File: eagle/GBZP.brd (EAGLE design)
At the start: 69.5 x 114.2 mm, 44 parts, among them CN1 Battery Connection, J1 AUDIO_JACK_3.5MM_SMD, U4 LM4875, X2 HEADPHONE

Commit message: updates
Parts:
- removed C1: 10uF, adafruit:C0805
- removed C15, C18, C6, C7: 10u, rcl:C0805
- removed C17: 100n, rcl:C0805
- removed C5: 220n, rcl:C0805
- removed C8: 330n, rcl:C0805
- removed C9: 100uF, rcl:153CLV-0405
- removed R4: 270Ohm, adafruit:R0805
- removed R6: 150Ohm, adafruit:R0805
- removed R7: 27k, GBA:VOLUME
- removed R8: 270R, rcl:R0805
- removed R9: 100k, rcl:R0805
- removed SP2: SPEAKER, GBA:SPEAKER
- removed U4: LM4875, texas:SOIC8
- removed X2: HEADPHONE, GBA:HEADPHONE
- added C10, C11: 100nF, adafruit:C0805
- added C12: 10uF, adafruit:C0805
- added R10: 27k, GBA:VOLUME
- added U1: LM4875, texas:SOIC8
- C2: value 10uF -> 100uF; device adafruit:C0805 -> SparkFun-Capacitors:NIC_10X10.5_CAP
- C3: value 33nF -> 220nF
- C4: value 33nF -> 330nF
- R5: value 150Ohm -> 270Ohm
- moved SP1 117.5 mm to (91.0, 70.0)
- moved C2 106.2 mm to (105.0, 97.0), flipped to the top
- moved R5 61.8 mm to (86.0, 58.0), flipped to the top, turned to 0 degrees
- moved C3 55.9 mm to (86.0, 52.0), flipped to the top, turned to 0 degrees
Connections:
- removed net 5V: C15.1, C17.1, C18.1, C7.2, R7.5, R9.2, U4.1
- removed net N$11: C6.1, U4.7
- removed net N$13: C9.-, X2.L, X2.R
- removed net N$14: C9.+, SP2.1, U4.5
- removed net N$15: SP2.2, U4.8
- removed net N$16: R9.1, U4.3, X2.2
- removed net N$3: C2.1, C3.2, R4.2, R5.2
- removed net N$5: C5.1, C8.1, R8.2
- removed net N$8: R7.3, U4.4
- removed net N$9: C5.2, U4.2
- new net BYP: C10.1, U1.7
- new net DC_VOL: R10.3, U1.4
- new net HEADPHONES: J1.RING, J1.TIP, R5.1, U1.3
- new net VIN: C3.1, U1.2
- new net VOUT1: C2.+, SP1.P$1, U1.5
- new net VOUT2: SP1.P$2, U1.8
- net GND: now also C10.2, R10.1, U1.6; no longer C15.2, C17.2, C18.2, C3.1, C6.2, C7.1, C8.2, R5.1, R6.2, R7.1, U4.6, X2.1, X2.GND
- net N$1: now also C2.-, J1.RSH, J1.TSH; no longer C1.2, J1.RING
- net N$2: now also C3.2, C4.2, R3.2; no longer C2.2, J1.TIP
- net N$4: now also C11.2, C12.2, U1.1; no longer C1.1, C4.2, R3.2, R6.1
- net PWM: no longer R8.1
- net PWM_LEFT: no longer R4.1
- net SWITCH_OUT+: now also C11.1, C12.1, R10.5, R5.2
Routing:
- net N$2: track 18.3 -> 0.00 mm
- net N$1: track 13.4 -> 0.00 mm
- net N$4: track 6.45 -> 0.00 mm
- net N$3: track 6.45 -> 0.00 mm
- net PWM_LEFT: track 80.4 -> 77.4 mm

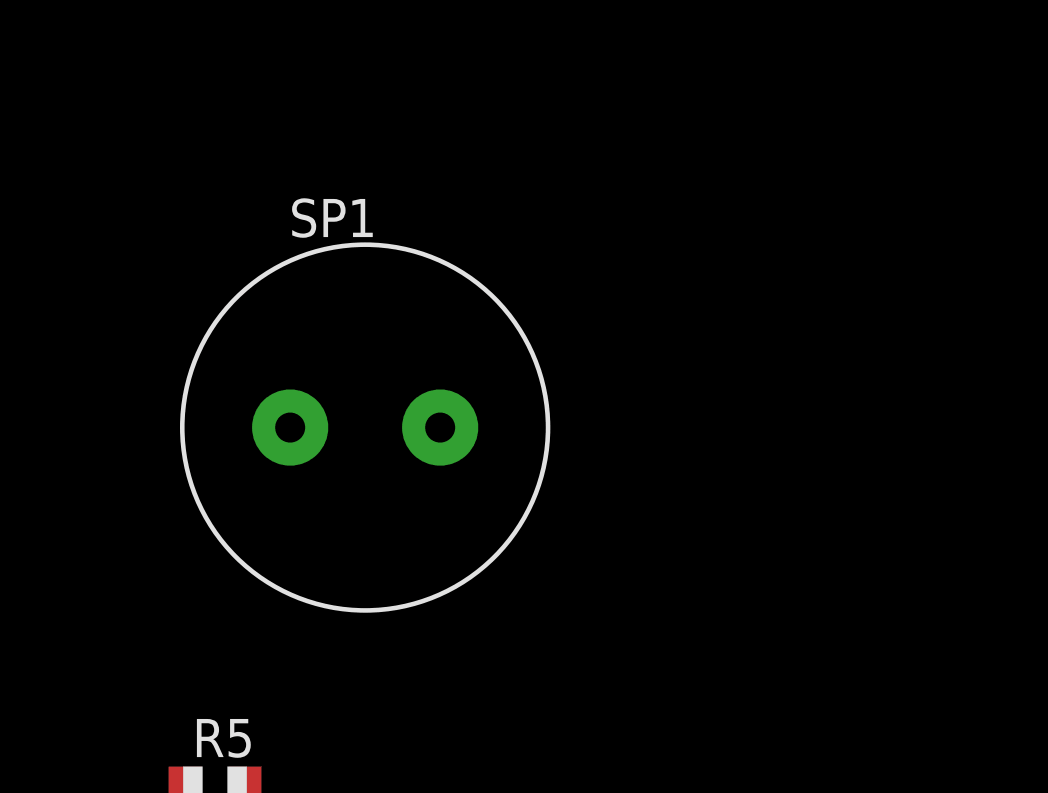
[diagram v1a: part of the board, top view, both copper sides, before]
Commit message: added LM4875
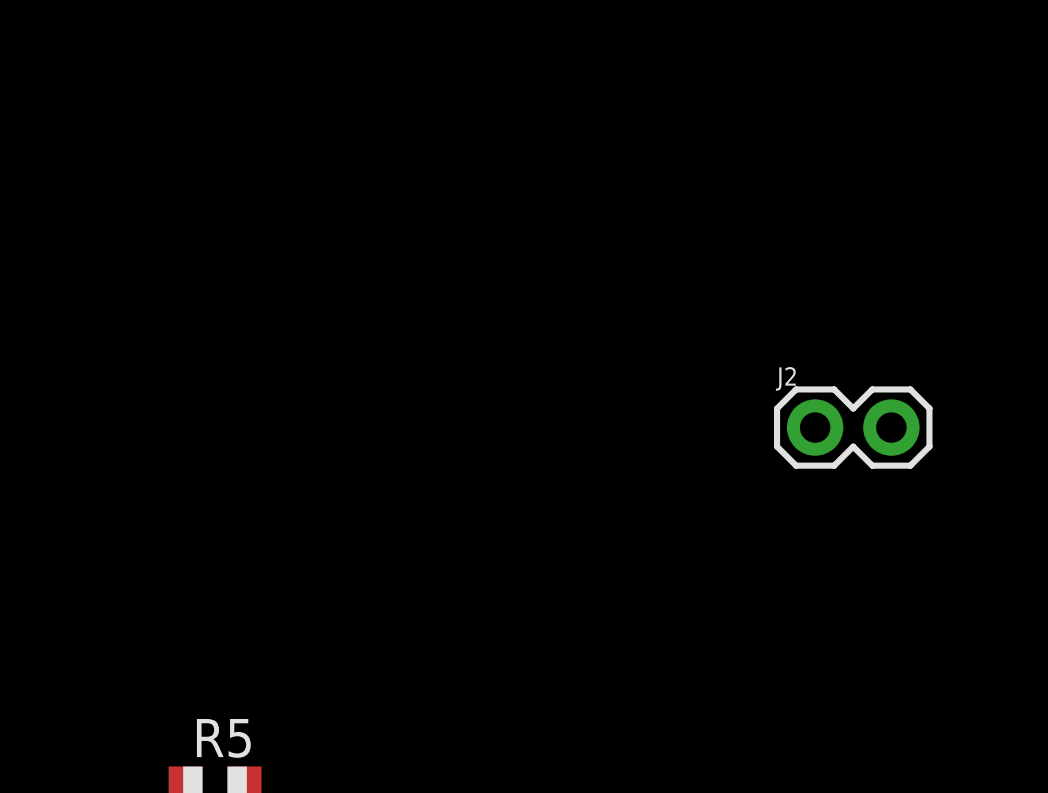
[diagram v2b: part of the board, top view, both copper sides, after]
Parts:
- removed SP1: SPEAKER/PS12, adafruit:PS12
- added J2: (no value), SparkFun-Connectors:1X02
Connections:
- net VOUT1: now also J2.1; no longer SP1.P$1
- net VOUT2: now also J2.2; no longer SP1.P$2
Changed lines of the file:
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@@
 <attribute name="PROD_ID" value="SWCH-10651" x="11.1" y="111.5" size="1.778" layer="28" rot="MR180" display="off"/>
 </element>
-<element name="SP1" library="adafruit" library_urn="urn:adsk.eagle:library:420" package="PS12" value="SPEAKER/PS12" x="91" y="70"/>
 <element name="C2" library="SparkFun-Capacitors" package="NIC_10X10.5_CAP" value="100uF" x="105" y="97">
 <attribute name="PROD_ID" value="CAP-08362" x="105" y="97" size="1.778" layer="27" display="off"/>
@@
 <element name="C11" library="adafruit" library_urn="urn:adsk.eagle:library:420" package="C0805" value="100nF" x="86" y="10"/>
 <element name="C12" library="adafruit" library_urn="urn:adsk.eagle:library:420" package="C0805" value="10uF" x="86" y="4"/>
+<element name="J2" library="SparkFun-Connectors" library_urn="urn:adsk.eagle:library:513" package="1X02" package3d_urn="urn:adsk.eagle:package:38039/1" value="" x="106" y="70"/>
 </elements>
 <signals>
@@
 <contactref element="C2" pad="+"/>
 <contactref element="U1" pad="5"/>
-<contactref element="SP1" pad="P$1"/>
+<contactref element="J2" pad="1"/>
 <wire x1="89.905" y1="99.6" x2="109.5" y2="97" width="0" layer="19" extent="1-1"/>
-<wire x1="88.5" y1="70" x2="89.905" y2="99.6" width="0" layer="19" extent="1-1"/>
+<wire x1="106" y1="70" x2="109.5" y2="97" width="0" layer="19" extent="1-1"/>
 </signal>
 <signal name="N$2">
@@
 <contactref element="C4" pad="2"/>
 <contactref element="C3" pad="2"/>
-<contactref element="C3" pad="2"/>
 <wire x1="30" y1="14" x2="86.85" y2="52" width="0" layer="19" extent="1-16"/>
 <wire x1="30.15" y1="12" x2="30" y2="14" width="0" layer="19" extent="16-16"/>
@@
 <signal name="VOUT2">
 <contactref element="U1" pad="8"/>
-<contactref element="SP1" pad="P$2"/>
-<wire x1="93.5" y1="70" x2="86.095" y2="99.6" width="0" layer="19" extent="1-1"/>
+<contactref element="J2" pad="2"/>
+<wire x1="108.54" y1="70" x2="86.095" y2="99.6" width="0" layer="19" extent="1-1"/>
 </signal>
 <signal name="HEADPHONES">

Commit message: headphones
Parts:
- C2: value 100uF -> 10uF; device SparkFun-Capacitors:NIC_10X10.5_CAP -> SparkFun-Capacitors:EIA3216
- moved U1 110.1 mm to (18.0, 12.0), flipped to the bottom, turned to 90 degrees
- moved R10 100.2 mm to (12.0, 68.0), flipped to the bottom, turned to 270 degrees
- moved C2 99.6 mm to (48.0, 15.3), flipped to the bottom, turned to 270 degrees
- moved R5 94.7 mm to (7.50, 5.00), flipped to the bottom, turned to 270 degrees
- moved C3 86.0 mm to (14.0, 5.00), flipped to the bottom, turned to 270 degrees
- moved J2 84.2 mm to (48.0, 9.00), flipped to the bottom, turned to 270 degrees
- moved C10 70.1 mm to (25.0, 11.4), flipped to the bottom, turned to 180 degrees
- moved C12 69.5 mm to (16.5, 5.00), flipped to the bottom, turned to 90 degrees
- moved C11 67.2 mm to (19.0, 5.00), flipped to the bottom, turned to 90 degrees
- moved R3 23.3 mm to (9.50, 5.00), turned to 270 degrees
- moved C4 20.7 mm to (11.5, 5.00), turned to 270 degrees
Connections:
- net N$1 renamed CAP_LINE_JACK
- net N$4 renamed CAP_LINE
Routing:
- net PWM_LEFT: track 77.4 -> 1.65 mm, vias 2 -> 0
- net SWITCH_OUT+: track 73.3 -> 139.5 mm
- net HEADPHONES: track 0.00 -> 53.8 mm
- net VOUT1: track 0.00 -> 32.3 mm, vias 0 -> 1
- net VOUT2: track 0.00 -> 31.0 mm, vias 0 -> 1
- net CAP_LINE_JACK: track 0.00 -> 24.9 mm
- net PWM: track 77.0 -> 92.0 mm, vias 0 -> 4
- net VIN: track 0.00 -> 8.92 mm
- net CAP_LINE: track 0.00 -> 7.85 mm
- net N$2: track 0.00 -> 4.65 mm
- net BYP: track 0.00 -> 3.55 mm
- net LEFT: track 63.8 -> 66.9 mm
